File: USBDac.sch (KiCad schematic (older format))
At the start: 23 parts, among them SW1 SPST, SW2 SPST, SW3 SPST, SW4 SPST, SW5 SPST, SW6 SPST, SW7 SPST, U1 PCM2707, X1 CRYSTAL, X2 USB-B-H

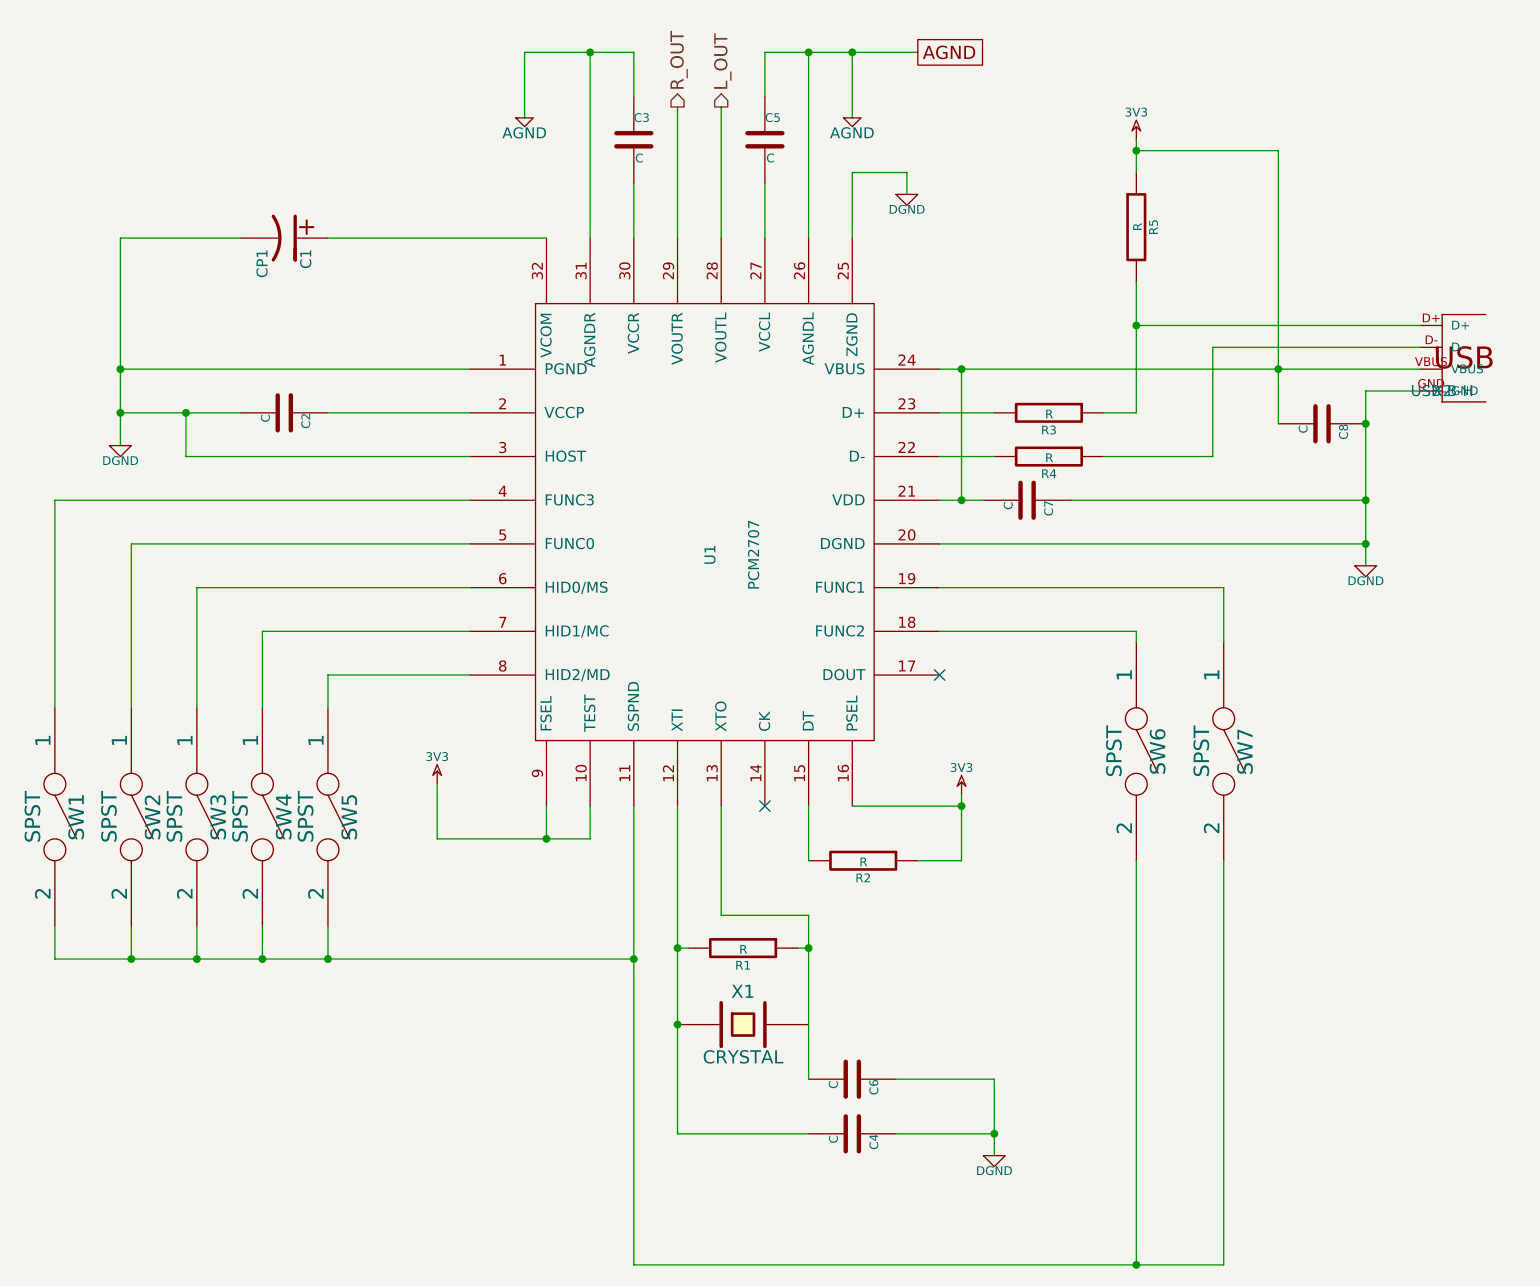
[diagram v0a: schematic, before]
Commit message: redrawn plus crossfeed, still needs PSU
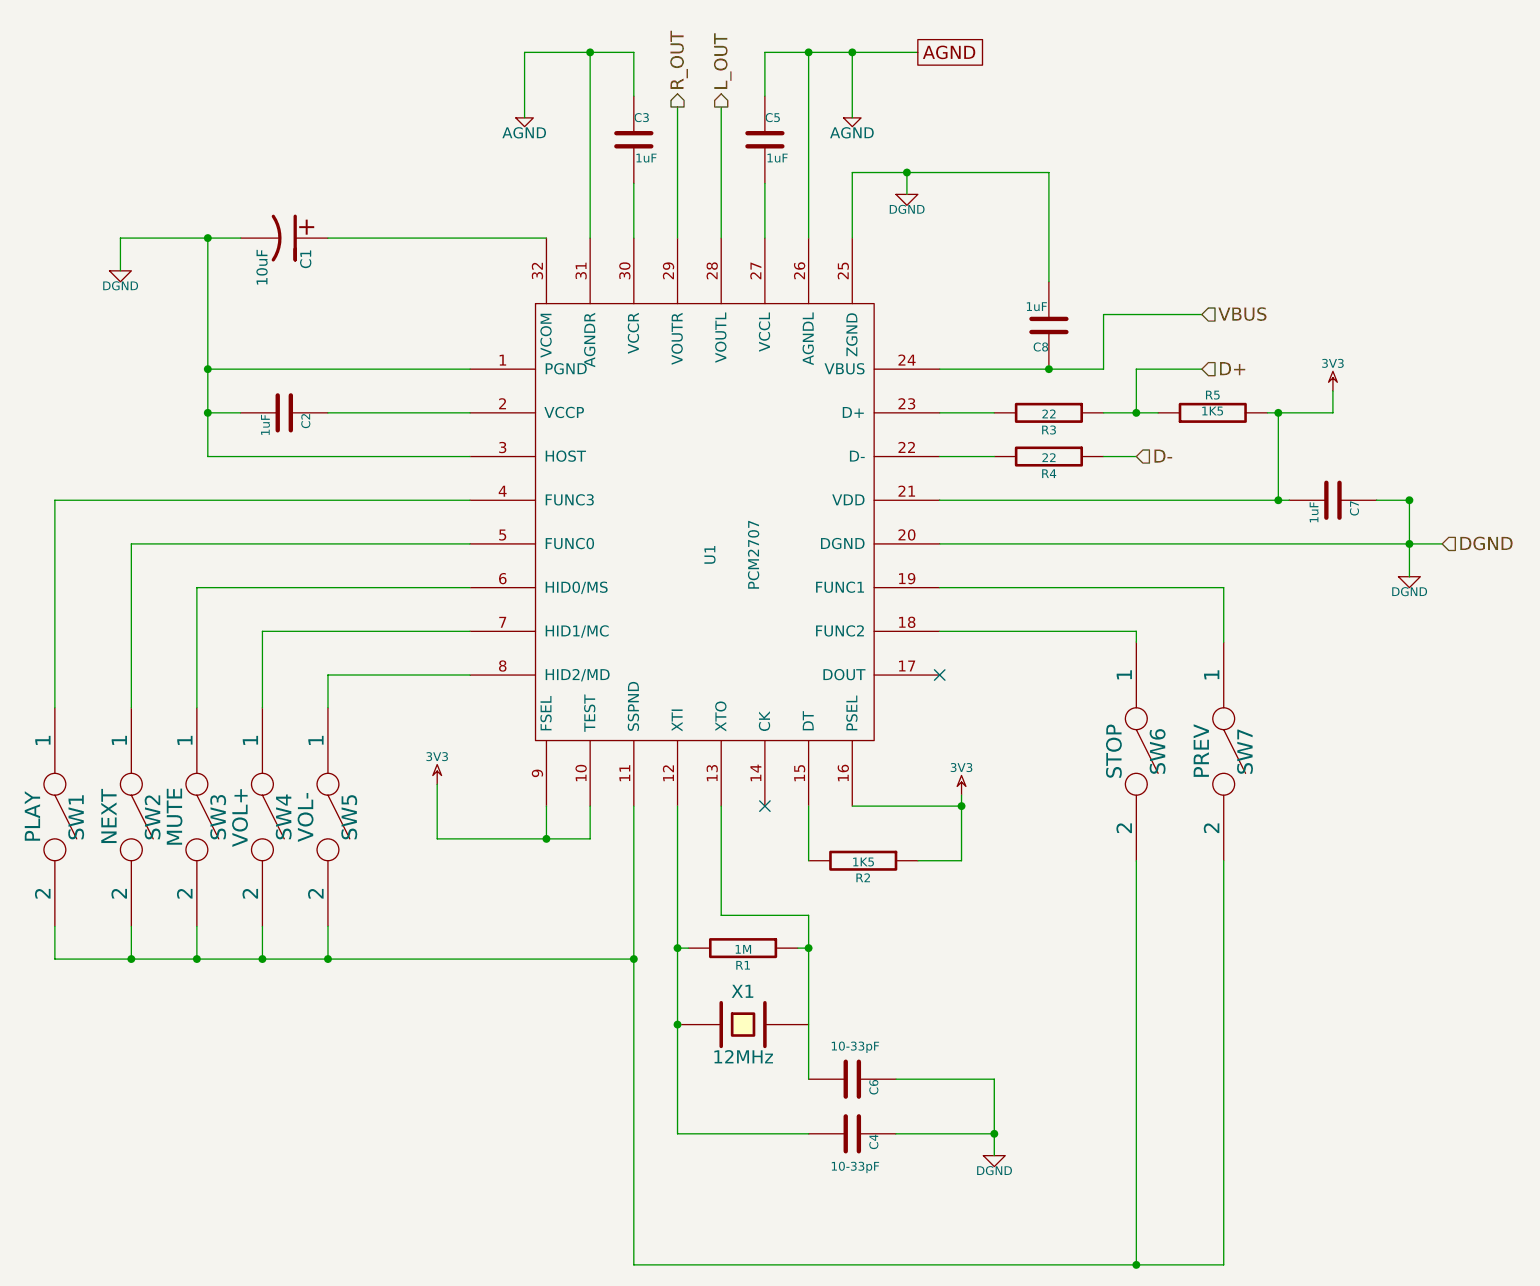
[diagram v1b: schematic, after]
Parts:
- removed X2: USB-B-H, con-usb-USB-B-H, symbol USB-B-H
- C1: value CP1 -> 10uF
- C2, C3, C5, C7, C8: value C -> 1uF
- C4, C6: value C -> 10-33pF
- R1: value R -> 1M
- R2, R5: value R -> 1K5
- R3, R4: value R -> 22
- SW1: value SPST -> PLAY
- SW2: value SPST -> NEXT
- SW3: value SPST -> MUTE
- SW4: value SPST -> VOL+
- SW5: value SPST -> VOL-
- SW6: value SPST -> STOP
- SW7: value SPST -> PREV
- X1: value CRYSTAL -> 12MHz
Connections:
- net 3V3: now also R5.2; no longer C8.2, R5.1, U1.24 (VBUS)
- net DGND: now also C8.2; no longer C8.1
- net D+: now reaches R3.1
- net D+: now also R5.1; no longer R5.2
- net D-: now reaches R4.1
- new net VBUS: C8.1, U1.24 (VBUS)
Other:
- moved on the sheet: C7, C8, R5
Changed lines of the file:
@@
 LIBS:audio
 LIBS:con-usb
+LIBS:v-reg
+LIBS:conn
 LIBS:2707-headphone-cache
 EELAYER 24 0
@@
 $Descr A4 11693 8268
 encoding utf-8
-Sheet 4 4
+Sheet 4 5
 Title "2707 Headphone DAC"
-Date "19 Jul 2014"
+Date "22 Jul 2014"
 Rev "0.1"
 Comp "Xav Paice"
@@
 P 5000 5350
 F 0 "X1" H 5000 5500 60  0000 C CNN
-F 1 "CRYSTAL" H 5000 5200 60  0000 C CNN
+F 1 "12MHz" H 5000 5200 60  0000 C CNN
 F 2 "" H 5000 5350 60  0000 C CNN
 F 3 "" H 5000 5350 60  0000 C CNN
@@
 P 2900 1750
 F 0 "C1" H 2950 1850 50  0000 L CNN
-F 1 "CP1" H 2950 1650 50  0000 L CNN
+F 1 "10uF" H 2950 1650 50  0000 L CNN
 F 2 "" H 2900 1750 60  0000 C CNN
 F 3 "" H 2900 1750 60  0000 C CNN
@@
 L DGND #PWR12
 U 1 1 53CB46FF
-P 2150 2700
-F 0 "#PWR12" H 2150 2700 40  0001 C CNN
-F 1 "DGND" H 2150 2630 40  0000 C CNN
-F 2 "" H 2150 2700 60  0000 C CNN
-F 3 "" H 2150 2700 60  0000 C CNN
-	1    2150 2700
+P 2150 1900
+F 0 "#PWR12" H 2150 1900 40  0001 C CNN
+F 1 "DGND" H 2150 1830 40  0000 C CNN
+F 2 "" H 2150 1900 60  0000 C CNN
+F 3 "" H 2150 1900 60  0000 C CNN
+	1    2150 1900
 	1    0    0    -1
 $EndComp
@@
 P 2900 2550
 F 0 "C2" H 2900 2650 40  0000 L CNN
-F 1 "C" H 2906 2465 40  0000 L CNN
+F 1 "1uF" H 2906 2465 40  0000 L CNN
 F 2 "" H 2938 2400 30  0000 C CNN
 F 3 "" H 2900 2550 60  0000 C CNN
@@
 	0    1    1    0
 $EndComp
-Wire Wire Line
-	2700 2550 2150 2550
-Connection ~ 2150 2550
 Wire Wire Line
 	3100 2550 3750 2550
@@
 P 2200 4400
 F 0 "SW2" H 2200 4500 70  0000 C CNN
-F 1 "SPST" H 2200 4300 70  0000 C CNN
+F 1 "NEXT" H 2200 4300 70  0000 C CNN
 F 2 "" H 2200 4400 60  0000 C CNN
 F 3 "" H 2200 4400 60  0000 C CNN
@@
 $EndComp
 Wire Wire Line
-	3750 2350 2150 2350
-Connection ~ 2150 2350
-Wire Wire Line
 	4100 1750 3100 1750
 Wire Wire Line
 	2700 1750 2150 1750
-Wire Wire Line
-	2150 1750 2150 2700
 $Comp
 L C C3
@@
 P 4500 1300
 F 0 "C3" H 4500 1400 40  0000 L CNN
-F 1 "C" H 4506 1215 40  0000 L CNN
+F 1 "1uF" H 4506 1215 40  0000 L CNN
 F 2 "" H 4538 1150 30  0000 C CNN
 F 3 "" H 4500 1300 60  0000 C CNN
@@
 P 5100 1300
 F 0 "C5" H 5100 1400 40  0000 L CNN
-F 1 "C" H 5106 1215 40  0000 L CNN
+F 1 "1uF" H 5106 1215 40  0000 L CNN
 F 2 "" H 5138 1150 30  0000 C CNN
 F 3 "" H 5100 1300 60  0000 C CNN
@@
 	5500 1750 5500 1450
 Wire Wire Line
-	5500 1450 5750 1450
+	5500 1450 6400 1450
 Wire Wire Line
 	5750 1450 5750 1550
@@
 P 1850 4400
 F 0 "SW1" H 1850 4500 70  0000 C CNN
-F 1 "SPST" H 1850 4300 70  0000 C CNN
+F 1 "PLAY" H 1850 4300 70  0000 C CNN
 F 2 "" H 1850 4400 60  0000 C CNN
 F 3 "" H 1850 4400 60  0000 C CNN
@@
 P 2500 4400
 F 0 "SW3" H 2500 4500 70  0000 C CNN
-F 1 "SPST" H 2500 4300 70  0000 C CNN
+F 1 "MUTE" H 2500 4300 70  0000 C CNN
 F 2 "" H 2500 4400 60  0000 C CNN
 F 3 "" H 2500 4400 60  0000 C CNN
@@
 P 2800 4400
 F 0 "SW4" H 2800 4500 70  0000 C CNN
-F 1 "SPST" H 2800 4300 70  0000 C CNN
+F 1 "VOL+" H 2800 4300 70  0000 C CNN
 F 2 "" H 2800 4400 60  0000 C CNN
 F 3 "" H 2800 4400 60  0000 C CNN
@@
 P 3100 4400
 F 0 "SW5" H 3100 4500 70  0000 C CNN
-F 1 "SPST" H 3100 4300 70  0000 C CNN
+F 1 "VOL-" H 3100 4300 70  0000 C CNN
 F 2 "" H 3100 4400 60  0000 C CNN
 F 3 "" H 3100 4400 60  0000 C CNN
@@
 Wire Wire Line
 	1850 2950 1850 3900
-Wire Wire Line
-	3750 2750 2450 2750
-Wire Wire Line
-	2450 2750 2450 2550
-Connection ~ 2450 2550
 $Comp
 L 3V3 #PWR13
@@
 P 5000 5000
 F 0 "R1" V 5080 5000 40  0000 C CNN
-F 1 "R" V 5007 5001 40  0000 C CNN
+F 1 "1M" V 5007 5001 40  0000 C CNN
 F 2 "" V 4930 5000 30  0000 C CNN
 F 3 "" H 5000 5000 30  0000 C CNN
@@
 P 5500 5850
 F 0 "C4" H 5500 5950 40  0000 L CNN
-F 1 "C" H 5506 5765 40  0000 L CNN
+F 1 "10-33pF" V 5650 5750 40  0000 L CNN
 F 2 "" H 5538 5700 30  0000 C CNN
 F 3 "" H 5500 5850 60  0000 C CNN
@@
 P 5500 5600
 F 0 "C6" H 5500 5700 40  0000 L CNN
-F 1 "C" H 5506 5515 40  0000 L CNN
+F 1 "10-33pF" V 5350 5500 40  0000 L CNN
 F 2 "" H 5538 5450 30  0000 C CNN
 F 3 "" H 5500 5600 60  0000 C CNN
@@
 P 5550 4600
 F 0 "R2" V 5630 4600 40  0000 C CNN
-F 1 "R" V 5557 4601 40  0000 C CNN
+F 1 "1K5" V 5557 4601 40  0000 C CNN
 F 2 "" V 5480 4600 30  0000 C CNN
 F 3 "" H 5550 4600 30  0000 C CNN
@@
 P 6800 4100
 F 0 "SW6" H 6800 4200 70  0000 C CNN
-F 1 "SPST" H 6800 4000 70  0000 C CNN
+F 1 "STOP" H 6800 4000 70  0000 C CNN
 F 2 "" H 6800 4100 60  0000 C CNN
 F 3 "" H 6800 4100 60  0000 C CNN
@@
 P 7200 4100
 F 0 "SW7" H 7200 4200 70  0000 C CNN
-F 1 "SPST" H 7200 4000 70  0000 C CNN
+F 1 "PREV" H 7200 4000 70  0000 C CNN
 F 2 "" H 7200 4100 60  0000 C CNN
 F 3 "" H 7200 4100 60  0000 C CNN
@@
 L C C7
 U 1 1 53CB47E5
-P 6300 2950
-F 0 "C7" H 6300 3050 40  0000 L CNN
-F 1 "C" H 6306 2865 40  0000 L CNN
-F 2 "" H 6338 2800 30  0000 C CNN
-F 3 "" H 6300 2950 60  0000 C CNN
-	1    6300 2950
-	0    1    1    0
-$EndComp
-Wire Wire Line
-	5900 2950 6100 2950
+P 7700 2950
+F 0 "C7" H 7700 3050 40  0000 L CNN
+F 1 "1uF" H 7706 2865 40  0000 L CNN
+F 2 "" H 7738 2800 30  0000 C CNN
+F 3 "" H 7700 2950 60  0000 C CNN
+	1    7700 2950
+	0    1    1    0
+$EndComp
 $Comp
 L DGND #PWR21
 U 1 1 53CB47ED
-P 7850 3250
-F 0 "#PWR21" H 7850 3250 40  0001 C CNN
-F 1 "DGND" H 7850 3180 40  0000 C CNN
-F 2 "" H 7850 3250 60  0000 C CNN
-F 3 "" H 7850 3250 60  0000 C CNN
-	1    7850 3250
-	1    0    0    -1
-$EndComp
-Connection ~ 6000 2950
-$Comp
-L USB-B-H X?
-U 1 1 53CB47F4
-P 8200 2450
-AR Path="/53CB47F4" Ref="X?"  Part="1"
-AR Path="/53CB00DB/53CB47F4" Ref="X2"  Part="1"
-F 0 "X2" H 8200 2450 50  0000 C CNN
-F 1 "USB-B-H" H 8200 2450 50  0000 C CNN
-F 2 "con-usb-USB-B-H" H 8200 2600 50  0001 C CNN
-F 3 "" H 8200 2450 60  0001 C CNN
-	1    8200 2450
-	1    0    0    -1
-$EndComp
-Wire Wire Line
-	5900 2350 8100 2350
-Wire Wire Line
-	6800 1950 6800 2550
-Wire Wire Line
-	6800 2150 8100 2150
-Wire Wire Line
-	7150 2750 7150 2250
-Wire Wire Line
-	7150 2250 8100 2250
-Wire Wire Line
-	6000 2950 6000 2350
-Connection ~ 6000 2350
+P 8050 3300
+F 0 "#PWR21" H 8050 3300 40  0001 C CNN
+F 1 "DGND" H 8050 3230 40  0000 C CNN
+F 2 "" H 8050 3300 60  0000 C CNN
+F 3 "" H 8050 3300 60  0000 C CNN
+	1    8050 3300
+	1    0    0    -1
+$EndComp
 $Comp
 L C C8
 U 1 1 53CB4802
-P 7650 2600
-F 0 "C8" H 7650 2700 40  0000 L CNN
-F 1 "C" H 7656 2515 40  0000 L CNN
-F 2 "" H 7688 2450 30  0000 C CNN
-F 3 "" H 7650 2600 60  0000 C CNN
-	1    7650 2600
-	0    1    1    0
-$EndComp
-Wire Wire Line
-	7450 1350 7450 2600
-Connection ~ 7450 2350
-Wire Wire Line
-	7850 2450 7850 3250
-Wire Wire Line
-	8100 2450 7850 2450
-Connection ~ 7850 2600
-Wire Wire Line
-	5900 3150 7850 3150
-Connection ~ 7850 3150
+P 6400 2150
+F 0 "C8" H 6400 2250 40  0000 L CNN
+F 1 "1uF" H 6406 2065 40  0000 L CNN
+F 2 "" H 6438 2000 30  0000 C CNN
+F 3 "" H 6400 2150 60  0000 C CNN
+	1    6400 2150
+	-1   0    0    1
+$EndComp
+Wire Wire Line
+	5900 3150 8200 3150
 $Comp
 L R R3
@@
 P 6400 2550
 F 0 "R3" V 6480 2550 40  0000 C CNN
-F 1 "R" V 6407 2551 40  0000 C CNN
+F 1 "22" V 6407 2551 40  0000 C CNN
 F 2 "" V 6330 2550 30  0000 C CNN
 F 3 "" H 6400 2550 30  0000 C CNN
@@
 P 6400 2750
 F 0 "R4" V 6480 2750 40  0000 C CNN
-F 1 "R" V 6407 2751 40  0000 C CNN
+F 1 "22" V 6407 2751 40  0000 C CNN
 F 2 "" V 6330 2750 30  0000 C CNN
 F 3 "" H 6400 2750 30  0000 C CNN
@@
 	5900 2550 6150 2550
 Wire Wire Line
-	6800 2550 6650 2550
-Wire Wire Line
 	5900 2750 6150 2750
-Wire Wire Line
-	6650 2750 7150 2750
-Wire Wire Line
-	6500 2950 7850 2950
-Connection ~ 7850 2950
-$Comp
-L 3V3 #PWR20
-U 1 1 53CB4824
-P 6800 1300
-F 0 "#PWR20" H 6800 1400 40  0001 C CNN
-F 1 "3V3" H 6800 1425 40  0000 C CNN
-F 2 "" H 6800 1300 60  0000 C CNN
-F 3 "" H 6800 1300 60  0000 C CNN
-	1    6800 1300
-	1    0    0    -1
-$EndComp
 $Comp
 L R R5
 U 1 1 53CB482A
-P 6800 1700
-F 0 "R5" V 6880 1700 40  0000 C CNN
-F 1 "R" V 6807 1701 40  0000 C CNN
-F 2 "" V 6730 1700 30  0000 C CNN
-F 3 "" H 6800 1700 30  0000 C CNN
-	1    6800 1700
-	1    0    0    -1
-$EndComp
-Wire Wire Line
-	6800 1450 6800 1300
-Connection ~ 6800 2150
-Wire Wire Line
-	7450 1350 6800 1350
-Connection ~ 6800 1350
+P 7150 2550
+F 0 "R5" V 7230 2550 40  0000 C CNN
+F 1 "1K5" V 7157 2551 40  0000 C CNN
+F 2 "" V 7080 2550 30  0000 C CNN
+F 3 "" H 7150 2550 30  0000 C CNN
+	1    7150 2550
+	0    -1   -1   0
+$EndComp
 NoConn ~ 5100 4350
 NoConn ~ 5900 3750
@@
 	5700 5600 6150 5600
 Connection ~ 6150 5850
+Text HLabel 8200 3150 2    60   Input ~ 0
+DGND
+Text HLabel 7100 2350 2    60   Input ~ 0
+D+
+Text HLabel 6800 2750 2    60   Input ~ 0
+D-
+Text HLabel 7100 2100 2    60   Input ~ 0
+VBUS
+Wire Wire Line
+	6400 1450 6400 1950
+Connection ~ 5750 1450
+Connection ~ 6400 2350
+Wire Wire Line
+	5900 2950 7500 2950
+Wire Wire Line
+	3750 2350 2550 2350
+Wire Wire Line
+	2550 1750 2550 2750
+Wire Wire Line
+	2550 2550 2700 2550
+Wire Wire Line
+	2150 1750 2150 1900
+Connection ~ 2550 1750
+Connection ~ 2550 2350
+Connection ~ 2550 2550
+Wire Wire Line
+	2550 2750 3750 2750
+Wire Wire Line
+	6800 2750 6650 2750
+Wire Wire Line
+	8050 2950 7900 2950
+Connection ~ 8050 3150
+Wire Wire Line
+	6650 2550 6900 2550
+Wire Wire Line
+	5900 2350 6650 2350
+Wire Wire Line
+	6650 2350 6650 2100
+Wire Wire Line
+	6650 2100 7100 2100
+Wire Wire Line
+	7100 2350 6800 2350
+Wire Wire Line
+	6800 2350 6800 2550
+Connection ~ 6800 2550
+Connection ~ 8050 2950
+Wire Wire Line
+	7400 2550 7700 2550
+Wire Wire Line
+	7450 2550 7450 2950
+Connection ~ 7450 2950
+Wire Wire Line
+	8050 2950 8050 3300
+$Comp
+L 3V3 #PWR?
+U 1 1 53CD4F89
+P 7700 2450
+F 0 "#PWR?" H 7700 2550 40  0001 C CNN
+F 1 "3V3" H 7700 2575 40  0000 C CNN
+F 2 "" H 7700 2450 60  0000 C CNN
+F 3 "" H 7700 2450 60  0000 C CNN
+	1    7700 2450
+	1    0    0    -1
+$EndComp
+Wire Wire Line
+	7700 2550 7700 2450
+Connection ~ 7450 2550
 $EndSCHEMATC
